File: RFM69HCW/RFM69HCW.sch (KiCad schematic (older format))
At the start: 1 part

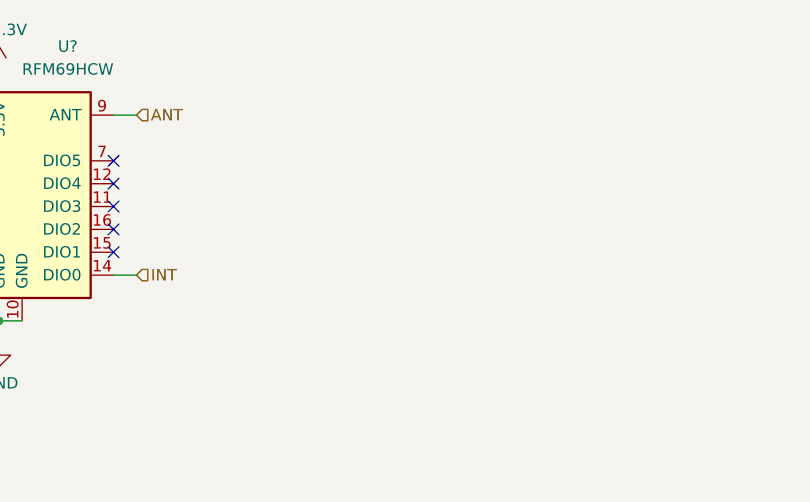
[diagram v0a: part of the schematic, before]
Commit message: updates to rfm and fix on pwr for stm
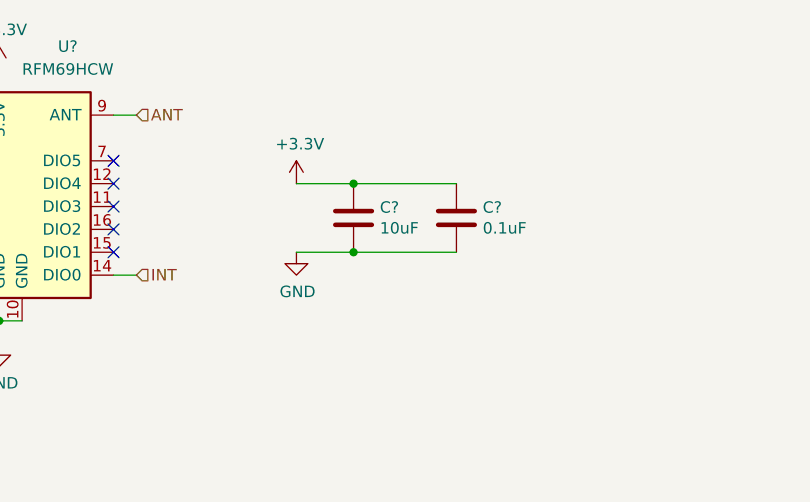
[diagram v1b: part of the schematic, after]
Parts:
- added C?: 10uF, symbol Device:C
- added C?: 0.1uF, symbol Device:C
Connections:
- net +3V3: now also C?.1, C?.1
- net GND: now also C?.2, C?.2
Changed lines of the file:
@@
 EESchema Schematic File Version 4
+LIBS:RFM69HCW-cache
 EELAYER 30 0
 EELAYER END
@@
 Text Notes 7200 6900 0    118  ~ 0
 RFM69HCW Hierarchical Block\n
+$Comp
+L power:+3.3V #PWR?
+U 1 1 5DE1AB32
+P 6600 3850
+F 0 "#PWR?" H 6600 3700 50  0001 C CNN
+F 1 "+3.3V" H 6615 4023 50  0000 C CNN
+F 2 "" H 6600 3850 50  0001 C CNN
+F 3 "" H 6600 3850 50  0001 C CNN
+	1    6600 3850
+	1    0    0    -1
+$EndComp
+$Comp
+L Device:C C?
+U 1 1 5DE1B04E
+P 6850 4000
+F 0 "C?" H 6965 4046 50  0000 L CNN
+F 1 "10uF" H 6965 3955 50  0000 L CNN
+F 2 "" H 6888 3850 50  0001 C CNN
+F 3 "~" H 6850 4000 50  0001 C CNN
+	1    6850 4000
+	1    0    0    -1
+$EndComp
+$Comp
+L Device:C C?
+U 1 1 5DE1B387
+P 7300 4000
+F 0 "C?" H 7415 4046 50  0000 L CNN
+F 1 "0.1uF" H 7415 3955 50  0000 L CNN
+F 2 "" H 7338 3850 50  0001 C CNN
+F 3 "~" H 7300 4000 50  0001 C CNN
+	1    7300 4000
+	1    0    0    -1
+$EndComp
+$Comp
+L power:GND #PWR?
+U 1 1 5DE1B548
+P 6600 4150
+F 0 "#PWR?" H 6600 3900 50  0001 C CNN
+F 1 "GND" H 6605 3977 50  0000 C CNN
+F 2 "" H 6600 4150 50  0001 C CNN
+F 3 "" H 6600 4150 50  0001 C CNN
+	1    6600 4150
+	1    0    0    -1
+$EndComp
+Wire Wire Line
+	6850 4150 6600 4150
+Connection ~ 6850 4150
+Wire Wire Line
+	6600 3850 6850 3850
+Connection ~ 6850 3850
+Wire Wire Line
+	6850 4150 7300 4150
+Wire Wire Line
+	6850 3850 7300 3850
 $EndSCHEMATC

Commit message: fix broken link in RFM69HCW schematic
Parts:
- U?: symbol RF_Module:RFM69HCW -> RF_AM_FM:RFM69HCW
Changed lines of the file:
@@
 EESchema Schematic File Version 4
-LIBS:RFM69HCW-cache
 EELAYER 30 0
 EELAYER END
@@
 $EndDescr
 $Comp
-L RF_Module:RFM69HCW U?
+L RF_AM_FM:RFM69HCW U?
 U 1 1 5DE2422E
 P 5300 3850
+AR Path="/5E51D058/5DE2422E" Ref="U?"  Part="1"
+AR Path="/5E51D40F/5DE2422E" Ref="U?"  Part="1"
+AR Path="/5E51D523/5DE2422E" Ref="U?"  Part="1"
+AR Path="/5DE2422E" Ref="U?"  Part="1"
 F 0 "U?" H 5600 4450 50  0000 C CNN
 F 1 "RFM69HCW" H 5600 4350 50  0000 C CNN
@@
 U 1 1 5DE24948
 P 5300 3350
+AR Path="/5E51D058/5DE24948" Ref="#PWR?"  Part="1"
+AR Path="/5E51D40F/5DE24948" Ref="#PWR?"  Part="1"
+AR Path="/5E51D523/5DE24948" Ref="#PWR?"  Part="1"
 F 0 "#PWR?" H 5300 3200 50  0001 C CNN
 F 1 "+3.3V" H 5315 3523 50  0000 C CNN
@@
 U 1 1 5DE24EBE
 P 5300 4550
+AR Path="/5E51D058/5DE24EBE" Ref="#PWR?"  Part="1"
+AR Path="/5E51D40F/5DE24EBE" Ref="#PWR?"  Part="1"
+AR Path="/5E51D523/5DE24EBE" Ref="#PWR?"  Part="1"
 F 0 "#PWR?" H 5300 4300 50  0001 C CNN
 F 1 "GND" H 5305 4377 50  0000 C CNN
@@
 U 1 1 5DE1AB32
 P 6600 3850
+AR Path="/5E51D058/5DE1AB32" Ref="#PWR?"  Part="1"
+AR Path="/5E51D40F/5DE1AB32" Ref="#PWR?"  Part="1"
+AR Path="/5E51D523/5DE1AB32" Ref="#PWR?"  Part="1"
 F 0 "#PWR?" H 6600 3700 50  0001 C CNN
 F 1 "+3.3V" H 6615 4023 50  0000 C CNN
@@
 U 1 1 5DE1B04E
 P 6850 4000
+AR Path="/5E51D058/5DE1B04E" Ref="C?"  Part="1"
+AR Path="/5E51D40F/5DE1B04E" Ref="C?"  Part="1"
+AR Path="/5E51D523/5DE1B04E" Ref="C?"  Part="1"
 F 0 "C?" H 6965 4046 50  0000 L CNN
 F 1 "10uF" H 6965 3955 50  0000 L CNN
@@
 U 1 1 5DE1B387
 P 7300 4000
+AR Path="/5E51D058/5DE1B387" Ref="C?"  Part="1"
+AR Path="/5E51D40F/5DE1B387" Ref="C?"  Part="1"
+AR Path="/5E51D523/5DE1B387" Ref="C?"  Part="1"
 F 0 "C?" H 7415 4046 50  0000 L CNN
 F 1 "0.1uF" H 7415 3955 50  0000 L CNN
@@
 U 1 1 5DE1B548
 P 6600 4150
+AR Path="/5E51D058/5DE1B548" Ref="#PWR?"  Part="1"
+AR Path="/5E51D40F/5DE1B548" Ref="#PWR?"  Part="1"
+AR Path="/5E51D523/5DE1B548" Ref="#PWR?"  Part="1"
 F 0 "#PWR?" H 6600 3900 50  0001 C CNN
 F 1 "GND" H 6605 3977 50  0000 C CNN

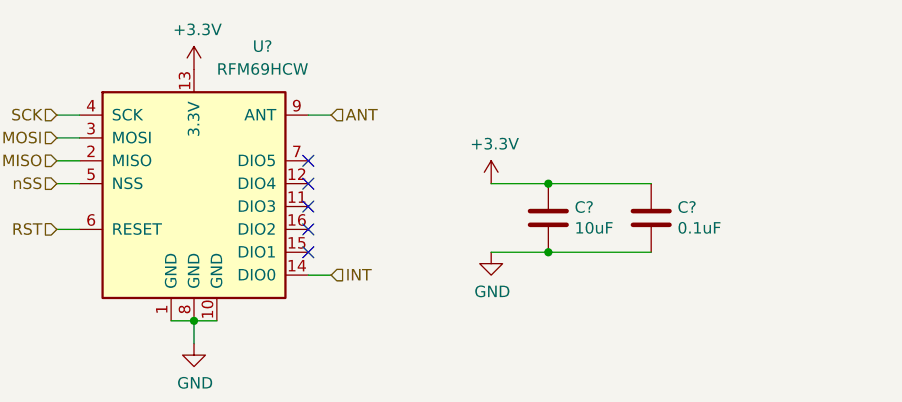
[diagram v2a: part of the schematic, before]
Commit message: update schematic fields, refdes numbers, and cleanup a couple schematics
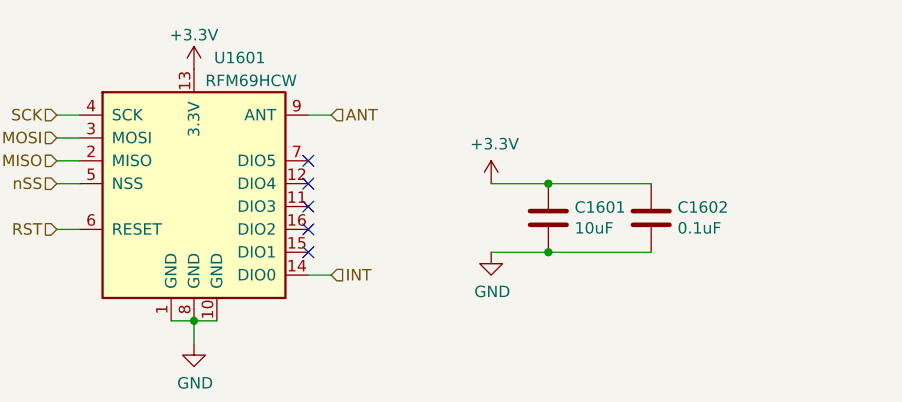
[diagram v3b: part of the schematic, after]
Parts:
- removed U?: RFM69HCW, symbol RF_AM_FM:RFM69HCW
- added U1601: RFM69HCW, RF_Module:HOPERF_RFM69HW, symbol RF_Module:RFM69HCW
- C1601: renamed from C?; footprint (none) -> Capacitor_SMD:C_0603_1608Metric; DIGIKEY (none) -> 490-13248-1-ND; MANF (none) -> GRM188R6YA106MA73D
- C1602: renamed from C?; footprint (none) -> Capacitor_SMD:C_0603_1608Metric; DIGIKEY (none) -> 399-1100-1-ND; MANF (none) -> C0603C104Z3VACTU
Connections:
- net +3V3: now also U1601.13 (3.3V)
- net ANT: now also U1601.9 (ANT)
- net GND: now also U1601.1 (GND), U1601.10 (GND), U1601.8 (GND)
- net INT: now also U1601.14 (DIO0)
- net MISO: now also U1601.2 (MISO)
- net MOSI: now also U1601.3 (MOSI)
- net RST: now also U1601.6 (RESET)
- net SCK: now also U1601.4 (SCK)
- net nSS: now also U1601.5 (NSS)
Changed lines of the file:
@@
 $EndDescr
-$Comp
-L RF_AM_FM:RFM69HCW U?
-U 1 1 5DE2422E
-P 5300 3850
-AR Path="/5E51D058/5DE2422E" Ref="U?"  Part="1"
-AR Path="/5E51D40F/5DE2422E" Ref="U?"  Part="1"
-AR Path="/5E51D523/5DE2422E" Ref="U?"  Part="1"
-AR Path="/5DE2422E" Ref="U?"  Part="1"
-F 0 "U?" H 5600 4450 50  0000 C CNN
-F 1 "RFM69HCW" H 5600 4350 50  0000 C CNN
-F 2 "" H 2000 5500 50  0001 C CNN
-F 3 "https://www.hoperf.com/data/upload/portal/20181127/5bfcb8284d838.pdf" H 2000 5500 50  0001 C CNN
-	1    5300 3850
-	1    0    0    -1
-$EndComp
 $Comp
 L power:+3.3V #PWR?
@@
 AR Path="/5E51D40F/5DE24948" Ref="#PWR?"  Part="1"
 AR Path="/5E51D523/5DE24948" Ref="#PWR?"  Part="1"
-F 0 "#PWR?" H 5300 3200 50  0001 C CNN
-F 1 "+3.3V" H 5315 3523 50  0000 C CNN
+AR Path="/5DE24948" Ref="#PWR01601"  Part="1"
+F 0 "#PWR01601" H 5300 3200 50  0001 C CNN
+F 1 "+3.3V" H 5300 3500 50  0000 C CNN
 F 2 "" H 5300 3350 50  0001 C CNN
 F 3 "" H 5300 3350 50  0001 C CNN
@@
 AR Path="/5E51D40F/5DE24EBE" Ref="#PWR?"  Part="1"
 AR Path="/5E51D523/5DE24EBE" Ref="#PWR?"  Part="1"
-F 0 "#PWR?" H 5300 4300 50  0001 C CNN
+AR Path="/5DE24EBE" Ref="#PWR01602"  Part="1"
+F 0 "#PWR01602" H 5300 4300 50  0001 C CNN
 F 1 "GND" H 5305 4377 50  0000 C CNN
 F 2 "" H 5300 4550 50  0001 C CNN
@@
 AR Path="/5E51D40F/5DE1AB32" Ref="#PWR?"  Part="1"
 AR Path="/5E51D523/5DE1AB32" Ref="#PWR?"  Part="1"
-F 0 "#PWR?" H 6600 3700 50  0001 C CNN
+AR Path="/5DE1AB32" Ref="#PWR01603"  Part="1"
+F 0 "#PWR01603" H 6600 3700 50  0001 C CNN
 F 1 "+3.3V" H 6615 4023 50  0000 C CNN
 F 2 "" H 6600 3850 50  0001 C CNN
@@
 AR Path="/5E51D40F/5DE1B04E" Ref="C?"  Part="1"
 AR Path="/5E51D523/5DE1B04E" Ref="C?"  Part="1"
-F 0 "C?" H 6965 4046 50  0000 L CNN
+AR Path="/5DE1B04E" Ref="C1601"  Part="1"
+F 0 "C1601" H 6965 4046 50  0000 L CNN
 F 1 "10uF" H 6965 3955 50  0000 L CNN
-F 2 "" H 6888 3850 50  0001 C CNN
+F 2 "Capacitor_SMD:C_0603_1608Metric" H 6888 3850 50  0001 C CNN
 F 3 "~" H 6850 4000 50  0001 C CNN
+F 4 "490-13248-1-ND" H 6850 4000 50  0001 C CNN "DIGIKEY"
+F 5 "GRM188R6YA106MA73D" H 6850 4000 50  0001 C CNN "MANF"
 	1    6850 4000
 	1    0    0    -1
@@
 AR Path="/5E51D40F/5DE1B387" Ref="C?"  Part="1"
 AR Path="/5E51D523/5DE1B387" Ref="C?"  Part="1"
-F 0 "C?" H 7415 4046 50  0000 L CNN
+AR Path="/5DE1B387" Ref="C1602"  Part="1"
+F 0 "C1602" H 7415 4046 50  0000 L CNN
 F 1 "0.1uF" H 7415 3955 50  0000 L CNN
-F 2 "" H 7338 3850 50  0001 C CNN
+F 2 "Capacitor_SMD:C_0603_1608Metric" H 7338 3850 50  0001 C CNN
 F 3 "~" H 7300 4000 50  0001 C CNN
+F 4 "399-1100-1-ND" H 7300 4000 50  0001 C CNN "DIGIKEY"
+F 5 "C0603C104Z3VACTU" H 7300 4000 50  0001 C CNN "MANF"
 	1    7300 4000
 	1    0    0    -1
@@
 AR Path="/5E51D40F/5DE1B548" Ref="#PWR?"  Part="1"
 AR Path="/5E51D523/5DE1B548" Ref="#PWR?"  Part="1"
-F 0 "#PWR?" H 6600 3900 50  0001 C CNN
+AR Path="/5DE1B548" Ref="#PWR01604"  Part="1"
+F 0 "#PWR01604" H 6600 3900 50  0001 C CNN
 F 1 "GND" H 6605 3977 50  0000 C CNN
 F 2 "" H 6600 4150 50  0001 C CNN
@@
 Wire Wire Line
 	6850 3850 7300 3850
+$Comp
+L RF_Module:RFM69HCW U1601
+U 1 1 5F9A3FCF
+P 5300 3850
+F 0 "U1601" H 5500 4400 50  0000 C CNN
+F 1 "RFM69HCW" H 5550 4300 50  0000 C CNN
+F 2 "RF_Module:HOPERF_RFM69HW" H 2000 5500 50  0001 C CNN
+F 3 "https://www.hoperf.com/data/upload/portal/20181127/5bfcb8284d838.pdf" H 2000 5500 50  0001 C CNN
+F 4 "RFM69HW-433S2" H 5300 3850 50  0001 C CNN "DIGIKEY"
+F 5 "RFM69HW-433S2-ND" H 5300 3850 50  0001 C CNN "MANF"
+	1    5300 3850
+	1    0    0    -1
+$EndComp
 $EndSCHEMATC
